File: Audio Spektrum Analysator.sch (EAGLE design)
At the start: 148 parts, among them IC1 LM324N, IC10 LM3914N, IC11 LM3914N, IC12 LM3914N, IC13 LM3914N, IC2 LM324N, IC3 LM324N, IC4 LM3914N, IC5 LM3914N, IC6 LM3914N, IC7 LM3914N, IC8 LM3914N, IC9 LM3914N, J2 DCJ0202, M1 ELECTRET_MICROPHON-F6050AP

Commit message: renamed
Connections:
- net +5V: now also TP1.TP; no longer TP3.TP
- net VER: now also TP3.TP; no longer TP1.TP
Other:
- moved on the sheet: TP1, TP3

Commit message: moved names
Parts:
- removed R8: 1k, rcl:R-EU_0207/7
- removed R9: 1k, resistor:R-EU_0207/7
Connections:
- removed net N$31: R10.S, R8.2
- removed net N$44: R11.S, R9.2
- net N$123: now also R11.S; no longer R9.1
- net N$5: now also R10.S; no longer R8.1
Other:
- moved on the sheet: C1, C2, C4, C5, IC1A, IC1B, J1, J2, R1, R10, R11, R2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

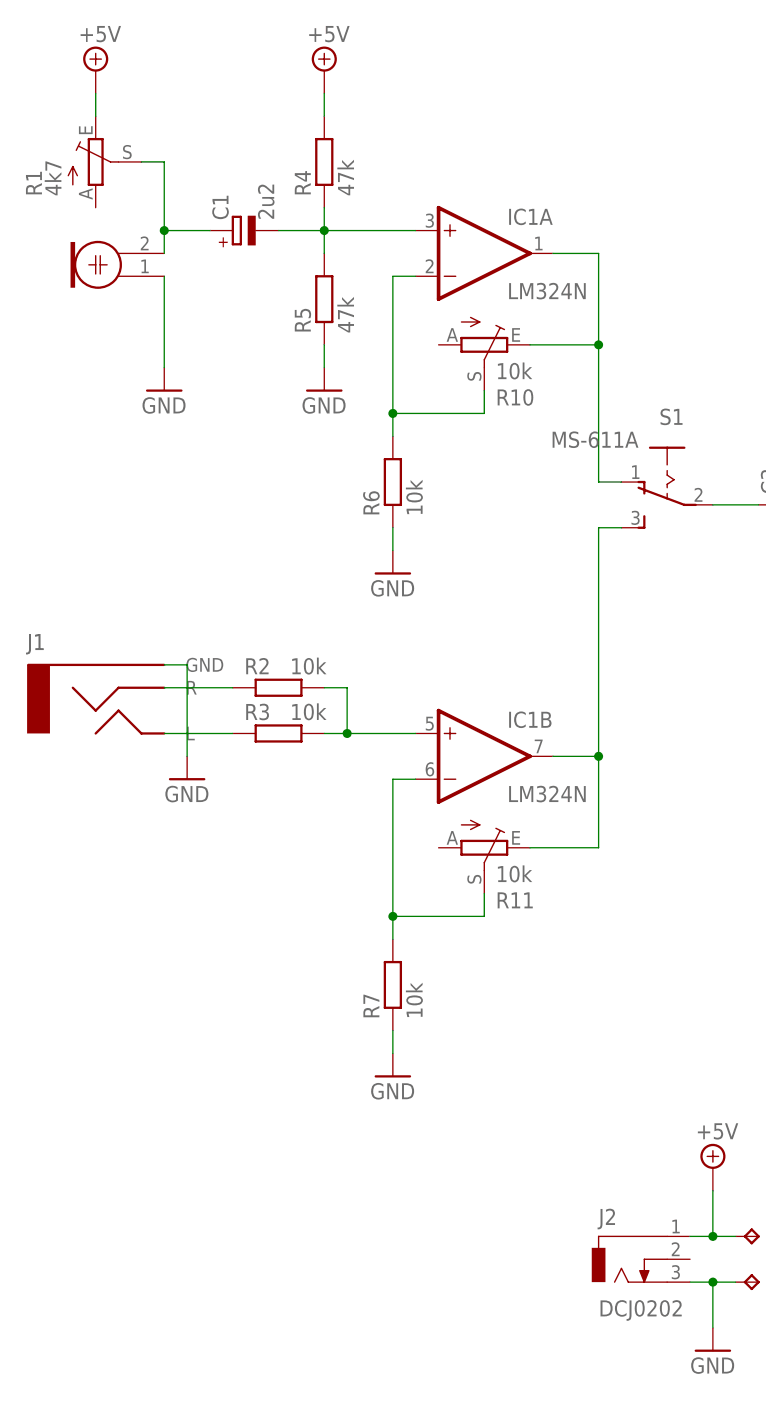
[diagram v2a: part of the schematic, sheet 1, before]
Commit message: worked on electret mic amp
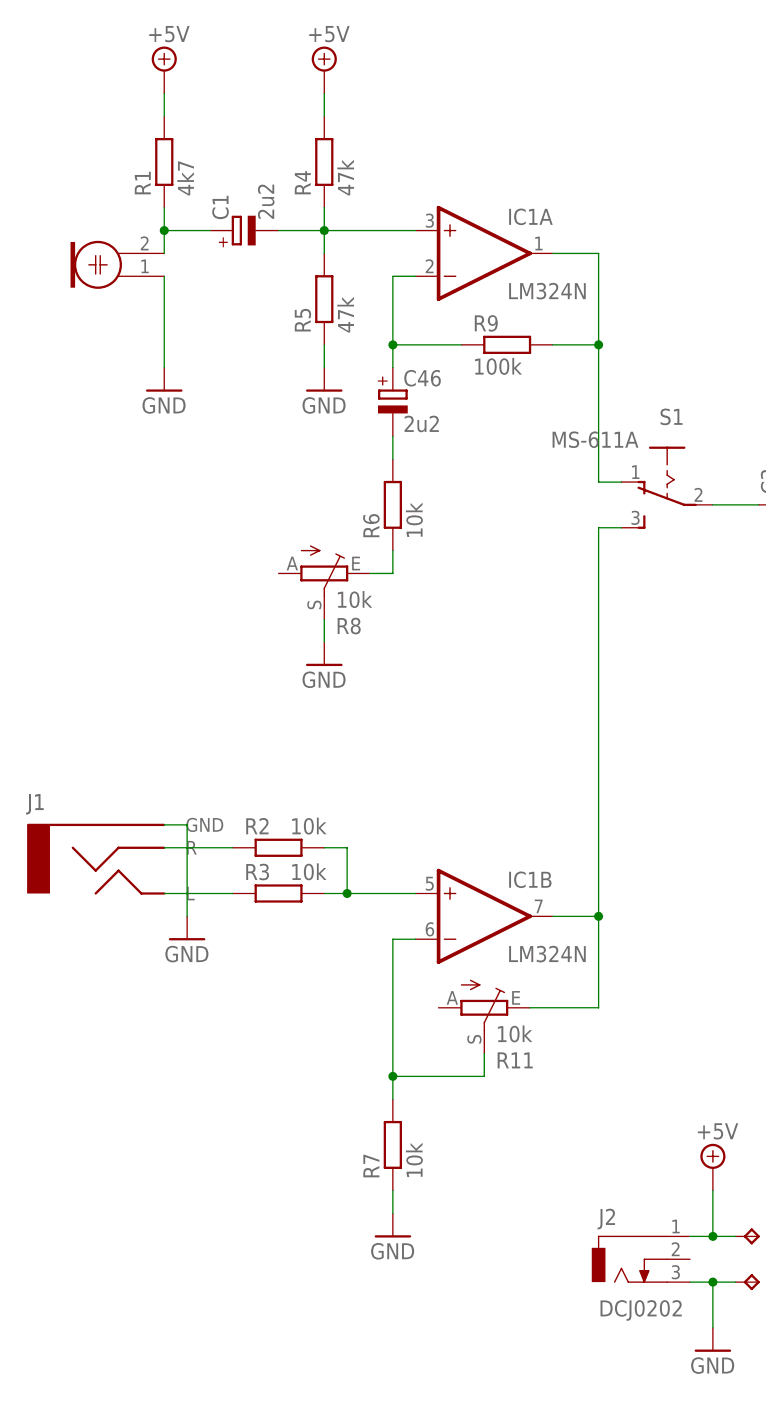
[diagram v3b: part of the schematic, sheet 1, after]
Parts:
- removed R10: 10k, pot:TRIM_EU-CA6V
- added C46: 2u2, resistor:CPOL-EUE2.5-5
- added R8: 10k, pot:TRIM_EU-CA6V
- added R9: 100k, rcl:R-EU_0207/7
- R1: device pot:TRIM_EU-CA6V -> rcl:R-EU_0207/7
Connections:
- new net N$31: C46.-, R6.2
- new net N$44: R6.1, R8.E
- net +5V: now also R1.2; no longer R1.E
- net GND: now also R8.S; no longer R6.1
- net N$13: now also R1.1; no longer R1.S
- net N$5: now also C46.+, R9.1; no longer R10.S, R6.2
- net N$6: now also R9.2; no longer R10.E
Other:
- moved on the sheet: IC1B, J1, R11, R2, R3, R6, R7

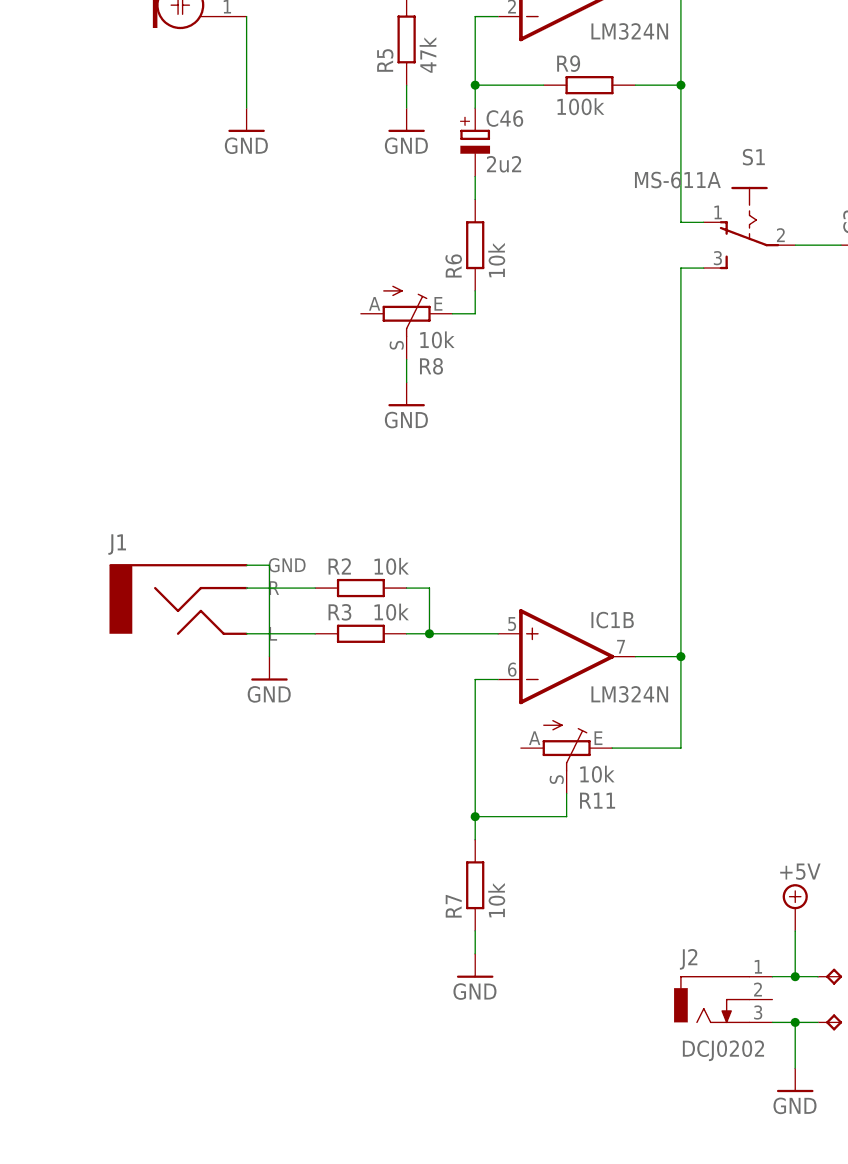
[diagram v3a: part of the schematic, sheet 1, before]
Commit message: edited preamp
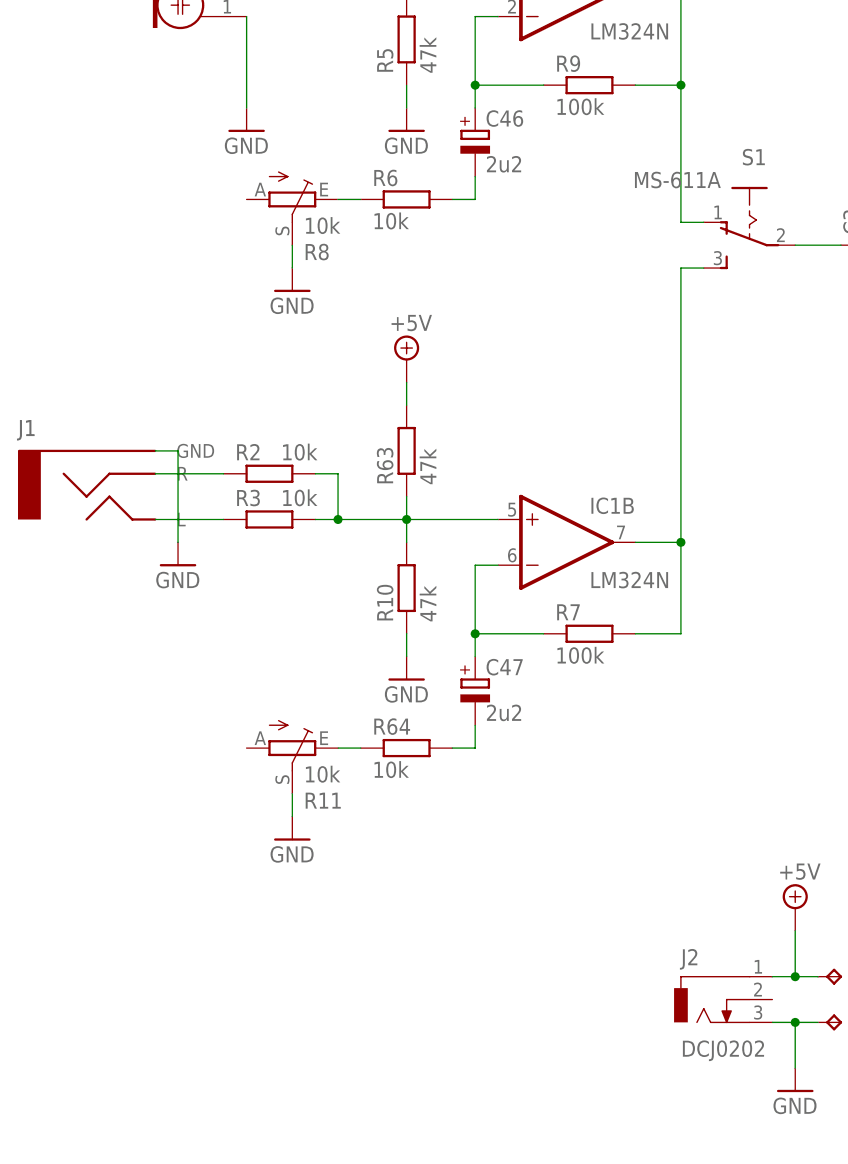
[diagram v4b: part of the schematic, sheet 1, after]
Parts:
- added C47: 2u2, resistor:CPOL-EUE2.5-5
- added R10, R63: 47k, rcl:R-EU_0207/7
- added R64: 10k, rcl:R-EU_0207/7
- R7: value 10k -> 100k
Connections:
- removed net N$123: IC1B.-IN, R11.S, R7.2
- new net N$57: C47.+, IC1B.-IN, R7.1
- new net N$70: C47.-, R64.2
- new net N$83: R11.E, R64.1
- net +5V: now also R63.2
- net GND: now also R10.1, R11.S; no longer R7.1
- net N$10: now also R7.2; no longer R11.E
- net N$3: now also R10.2, R63.1
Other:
- moved on the sheet: IC1B, J1, R11, R2, R3, R6, R7, R8

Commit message: edited reference circuit of LM3916s
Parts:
- removed R45: 1k2, resistor:R-EU_0207/7
- removed R48, R50, R52, R54, R56, R58, R60, R62: 7k5, resistor:R-EU_0207/7
- added R65: 1M, rcl:R-EU_0207/7
- added R66, R67: 100k, rcl:R-EU_0207/7
- added R68: 1k2, resistor:R-EU_0207/7
- R43: value 1k2 -> 20k
- R44: value 7k5 -> 20k
- R46: value 7k5 -> 1k2
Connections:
- removed net N$107: IC4.RHI, IC4.VR, R43.2
- removed net N$120: IC11.RHI, IC11.VR, R57.2
- removed net N$121: IC11.ADJ, R57.1, R58.2
- removed net N$127: IC12.RHI, IC12.VR, R59.2
- removed net N$128: IC12.ADJ, R59.1, R60.2
- removed net N$179: IC13.RHI, IC13.VR, R61.2
- removed net N$180: IC13.ADJ, R61.1, R62.2
- removed net N$82: IC10.ADJ, R55.1, R56.2
- removed net N$94: IC9.RHI, IC9.VR, R53.2
- removed net N$95: IC9.ADJ, R53.1, R54.2
- new net RHI: IC10.RHI, IC11.RHI, IC12.RHI, IC13.RHI, IC4.RHI, IC5.RHI, IC6.RHI, IC7.RHI, IC8.RHI, IC9.RHI, R43.1, R44.2
- net +5V: now also R43.2
- net GND: now also IC10.ADJ, IC11.ADJ, IC12.ADJ, IC13.ADJ, IC4.ADJ, IC5.ADJ, IC6.ADJ, IC7.ADJ, IC8.ADJ, IC9.ADJ, R47.1, R49.1, R51.1, R53.1, R55.1, R57.1, R59.1, R61.1, R65.1, R66.1, R67.1, R68.1; no longer R48.1, R50.1, R52.1, R54.1, R56.1, R58.1, R60.1, R62.1
- net N$108: now also IC4.VR, R68.2; no longer IC4.ADJ, R43.1, R44.2
- net N$29: no longer IC6.RHI
- net N$30: now also IC5.VR, R46.2; no longer IC6.ADJ, R47.1, R48.2
- net N$42: now also IC7.VR, R49.2; no longer IC5.RHI, IC5.VR, R45.2
- net N$43: now also IC8.VR, R51.2; no longer IC5.ADJ, R45.1, R46.2
- net N$55: now also IC10.VR, R55.2; no longer IC7.RHI, IC7.VR, R49.2
- net N$56: now also IC9.VR, R53.2; no longer IC7.ADJ, R49.1, R50.2
- net N$68: now also IC11.VR, R57.2; no longer IC8.RHI, IC8.VR, R51.2
- net N$69: now also IC12.VR, R59.2; no longer IC8.ADJ, R51.1, R52.2
- net N$81: now also IC13.VR, R61.2; no longer IC10.RHI, IC10.VR, R55.2
- net OUT1: now also R66.2
- net OUT2: now also R67.2
- net VER: now also R65.2
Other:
- moved on the sheet: C10, C11, R43, R44, R46, R47, R49, R51, R53, R55, R57, R59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

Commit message: started connecting Lm3916s
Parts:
- added R45, R48, R50, R52, R54, R56, R58, R60: 100k, rcl:R-EU_0207/7
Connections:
- net +5V renamed V+
- net GND: now also R45.1, R48.1, R50.1, R52.1, R54.1, R56.1, R58.1, R60.1
- net OUT10: now also R60.2
- net OUT3: now also R45.2
- net OUT4: now also R48.2
- net OUT5: now also R50.2
- net OUT6: now also R52.2
- net OUT7: now also R54.2
- net OUT8: now also R56.2
- net OUT9: now also R58.2
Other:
- moved on the sheet: C20, C21, C22, C23, C32, C33, C34, C35

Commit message: removed layers, further connected LM3916s
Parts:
- added C48: 1u, capacitor-wima:C5/5
- R11: value 10k -> 50k
- R64: value 10k -> 1k
- R7: value 100k -> 10k
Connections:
- net N$13: now also C1.-; no longer C1.+
- net N$4: now also C1.+; no longer C1.-
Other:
- note added: "RLOW offset must be compensated, maybe individually"
- note added: "consider using low leackage polypropylen capacitors"
- moved on the sheet: C1

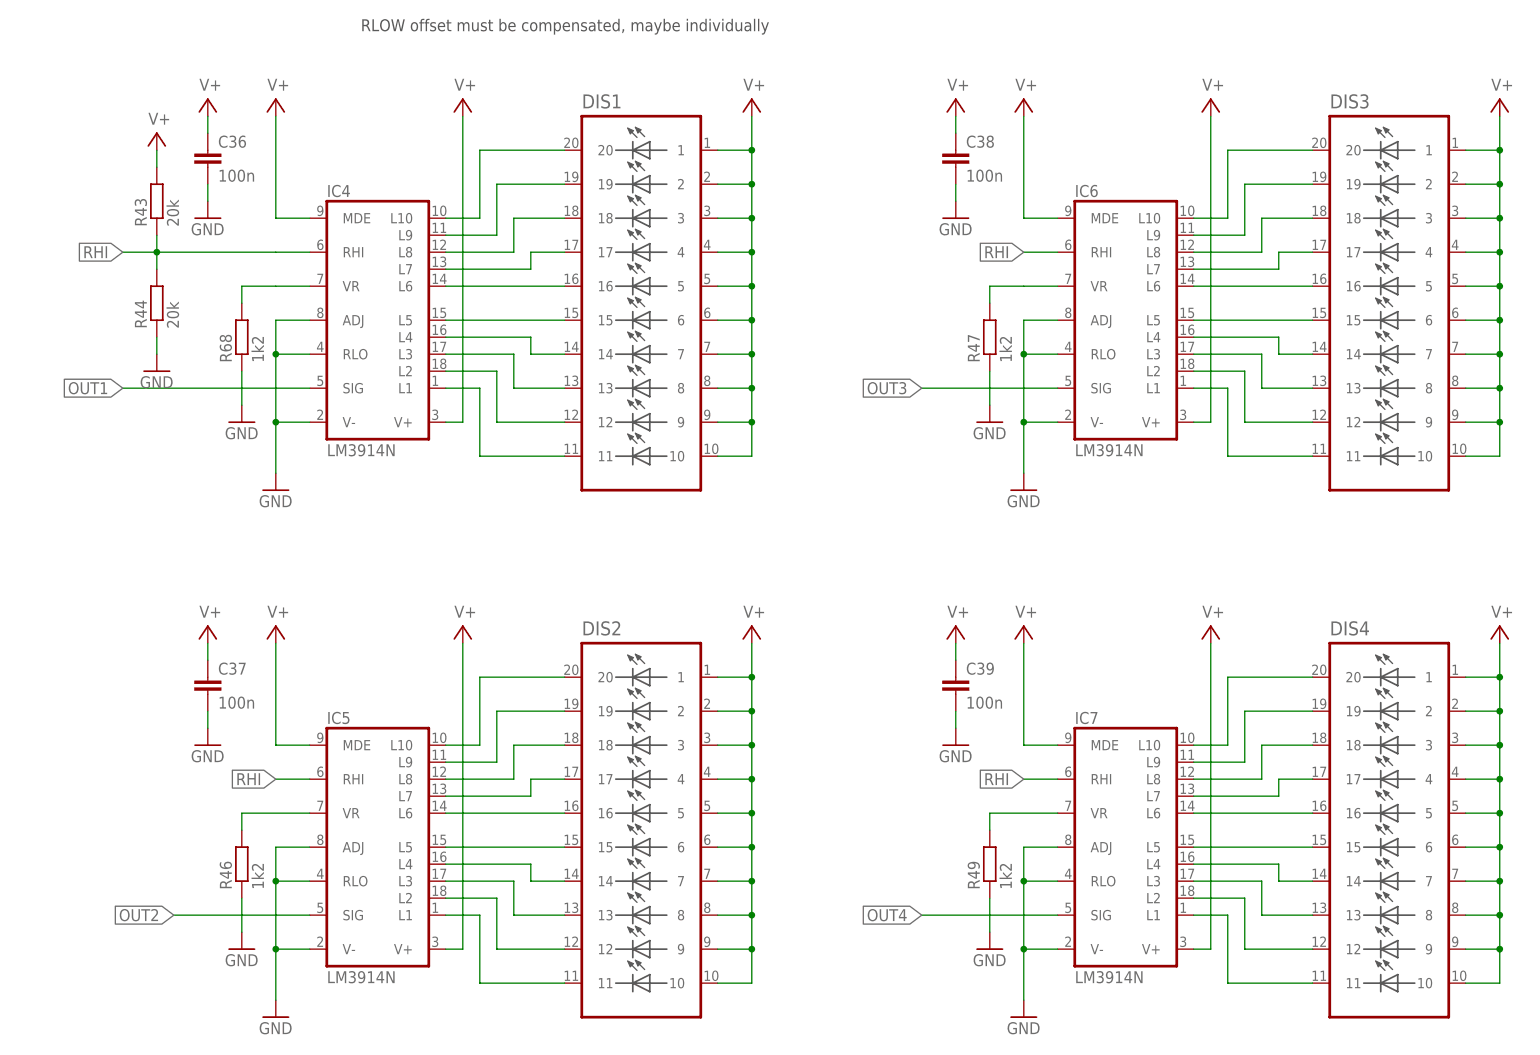
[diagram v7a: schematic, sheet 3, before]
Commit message: added RLO offest compensation in the schematic
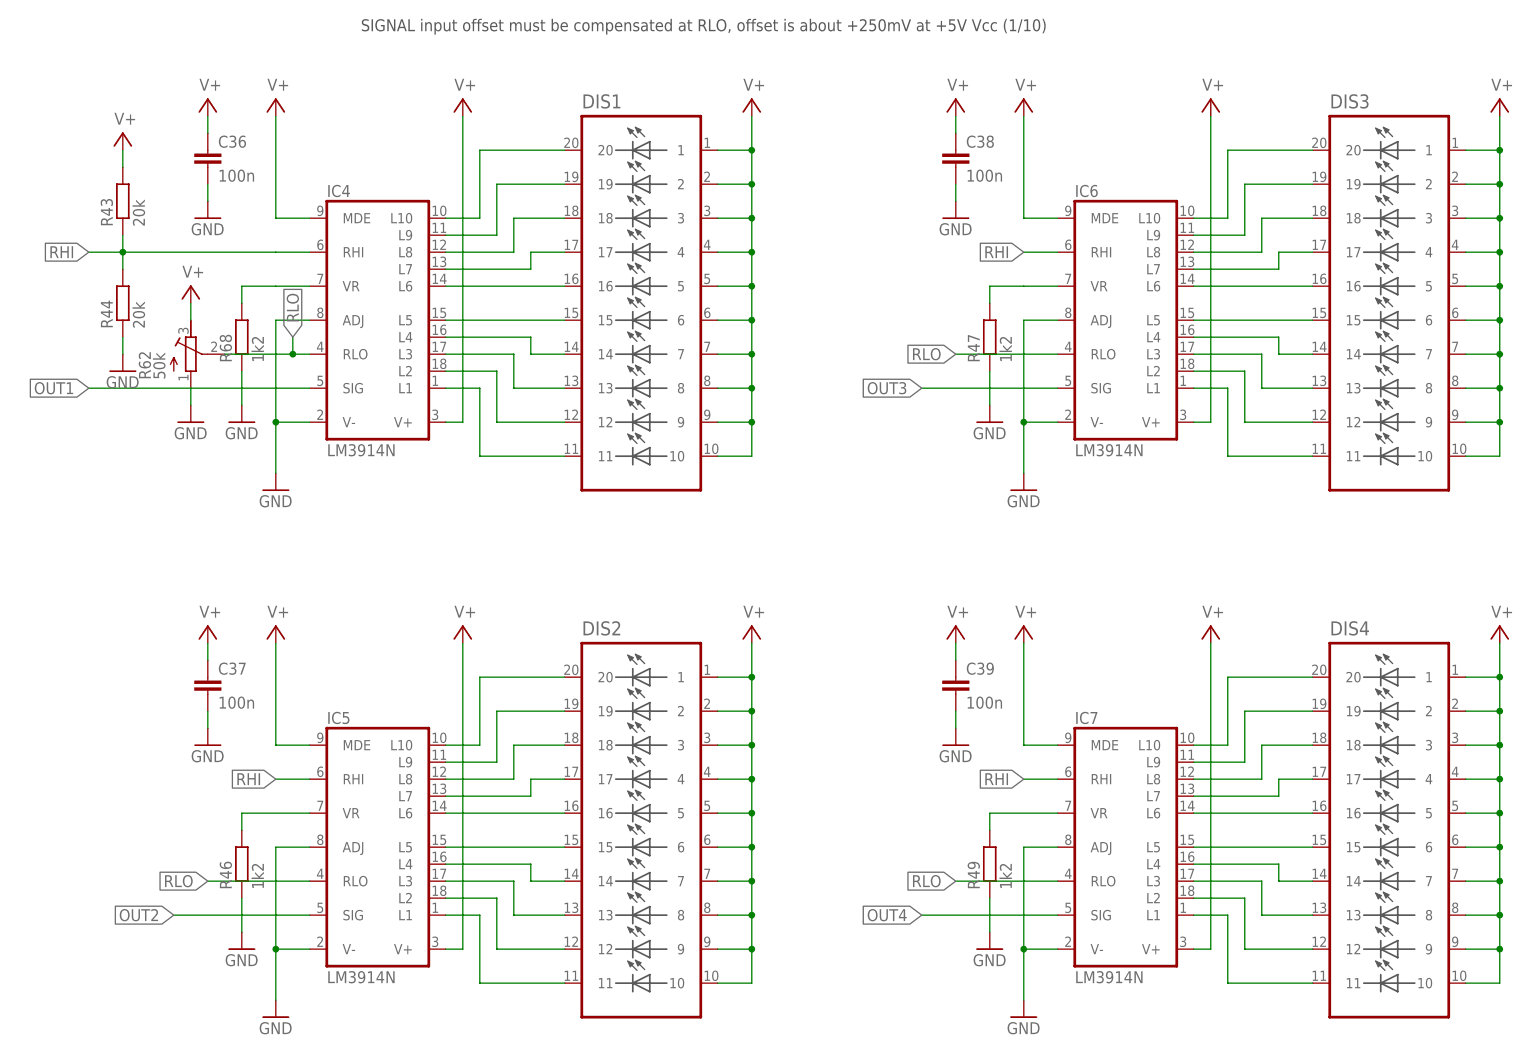
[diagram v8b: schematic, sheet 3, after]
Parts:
- added R62: 50k, resistor:R-TRIMM64W
- R11, R8: device pot:TRIM_EU-CA6V -> resistor:R-TRIMM64W
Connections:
- new net RLO: IC10.RLO, IC11.RLO, IC12.RLO, IC13.RLO, IC4.RLO, IC5.RLO, IC6.RLO, IC7.RLO, IC8.RLO, IC9.RLO, R62.S
- net GND: now also R62.A; no longer IC10.RLO, IC11.RLO, IC12.RLO, IC13.RLO, IC4.RLO, IC5.RLO, IC6.RLO, IC7.RLO, IC8.RLO, IC9.RLO
- net V+: now also R62.E
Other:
- note added: "SIGNAL input offset must be compensated at RLO, offset is about +250mV at +5V Vcc (1/10)"
- note removed: "RLOW offset must be compensated, maybe individually"
- moved on the sheet: R43, R44
